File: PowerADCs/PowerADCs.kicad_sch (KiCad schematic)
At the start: 28 parts, among them J1 I2C_STANDARDQWIIC, J2 Conn_01x02_Female, J3 Conn_01x10_Female, J4 Conn_01x10_Female, J6 Conn_01x02_Female, J7 Conn_01x02_Female, U1 MCP3428, U2 MCP3428, U3 INA219AxD, U4 SY6280AAC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

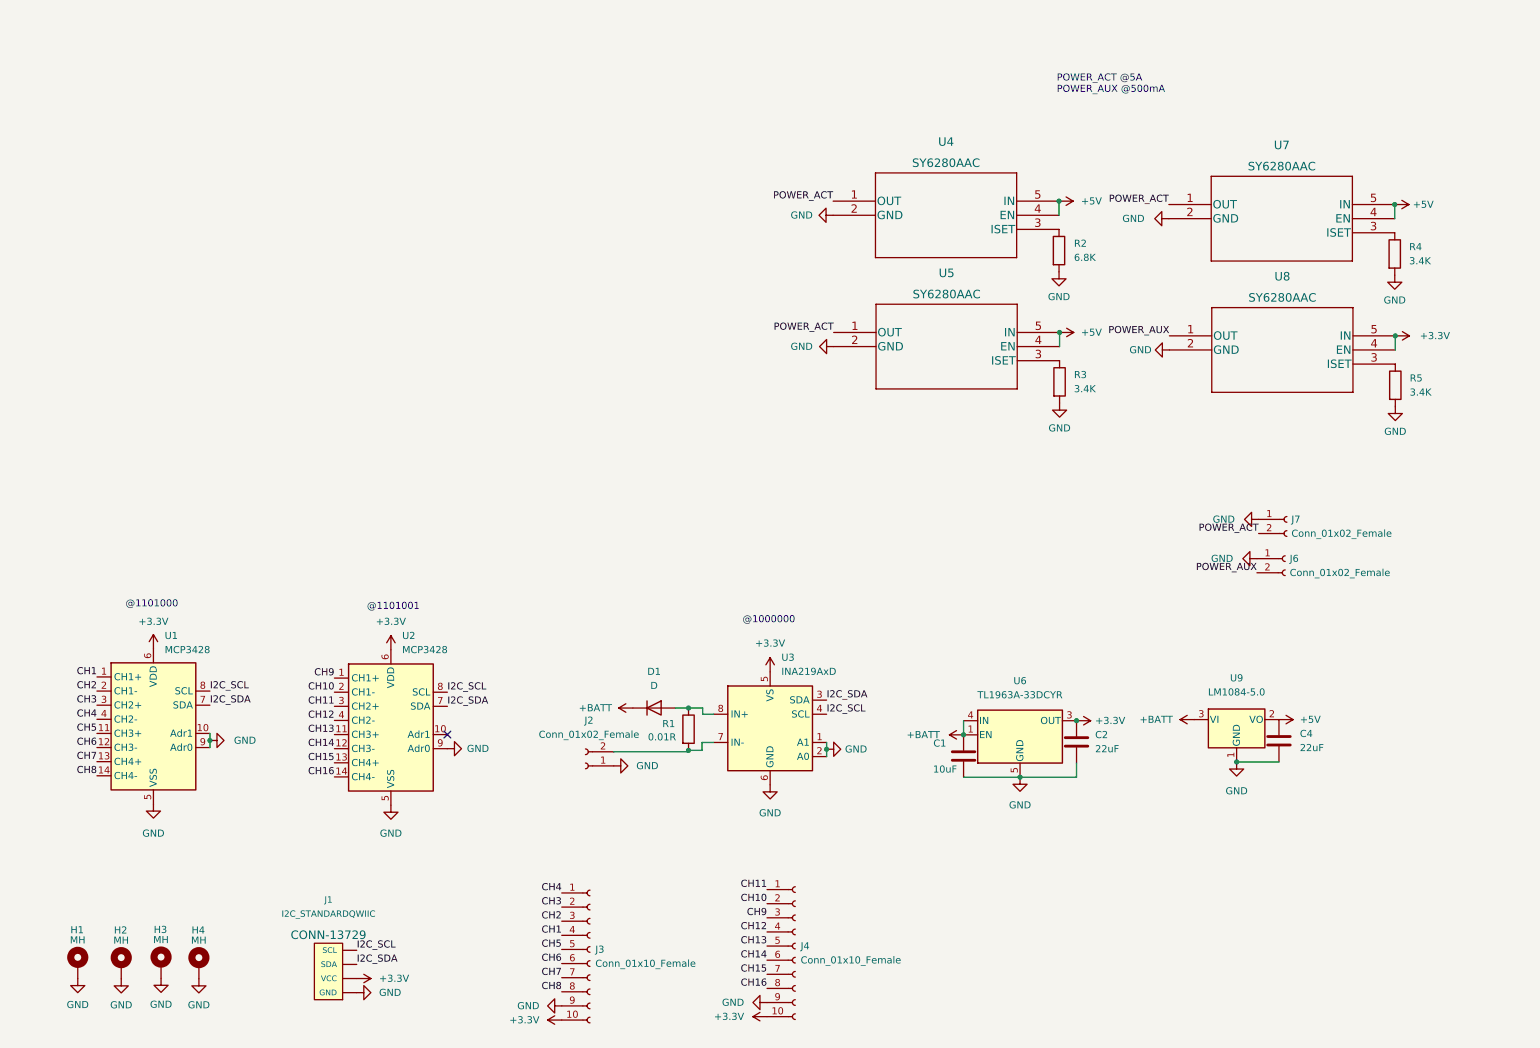
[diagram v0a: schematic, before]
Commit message: change ADC's and add seconde qwiic connector
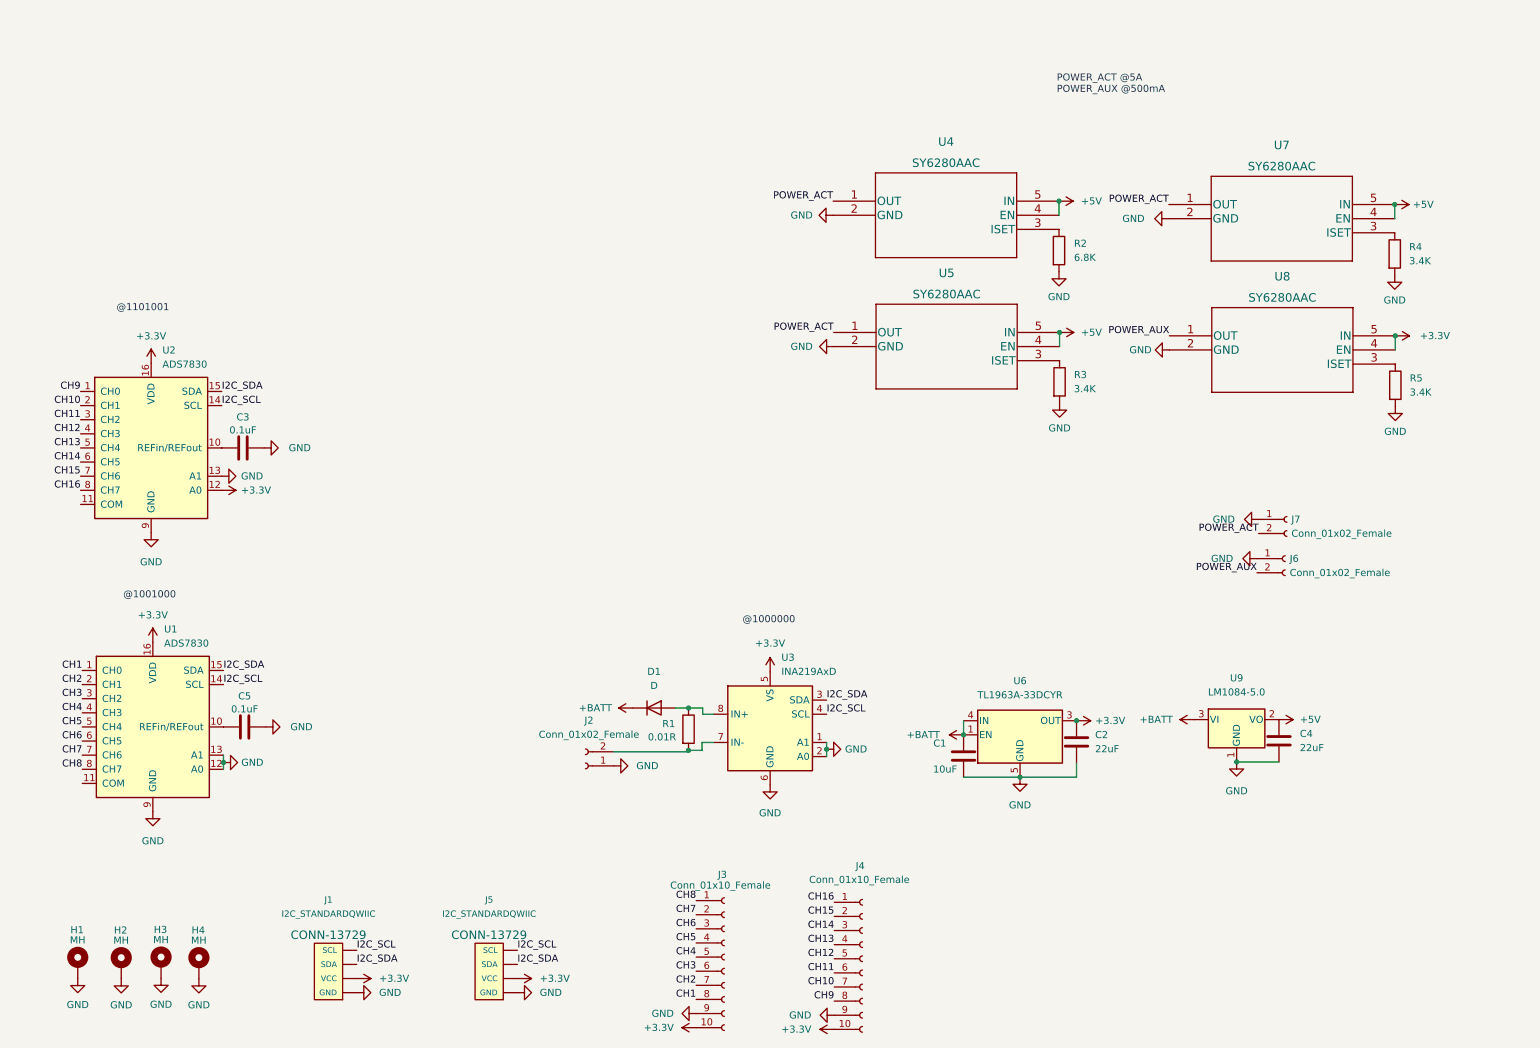
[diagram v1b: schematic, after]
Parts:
- removed U1, U2: MCP3428, Package_SO:TSSOP-14_4.4x5mm_P0.65mm, symbol Analog_ADC:MCP3428
- added C3, C5: 0.1uF, Capacitor_SMD:C_0402_1005Metric, symbol Device:C
- added J5: I2C_STANDARDQWIIC, Connectors:1X04_1MM_RA, symbol SparkFun-Connectors:I2C_STANDARDQWIIC
- added U1, U2: ADS7830, Package_SO:TSSOP-16_4.4x5mm_P0.65mm, symbol Analog_DAC:ADS7830
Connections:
- net +3V3: now also J5.2 (VCC), U1.16 (VDD), U2.12 (A0), U2.16 (VDD)
- net CH1: now also J3.8 (Pin_8), U1.1 (CH0); no longer J3.4 (Pin_4)
- net CH10: now also J4.7 (Pin_7), U2.2 (CH1); no longer J4.2 (Pin_2)
- net CH11: now also J4.6 (Pin_6), U2.3 (CH2); no longer J4.1 (Pin_1)
- net CH12: now also J4.5 (Pin_5), U2.4 (CH3); no longer J4.4 (Pin_4)
- net CH13: now also J4.4 (Pin_4), U2.5 (CH4); no longer J4.5 (Pin_5)
- net CH14: now also J4.3 (Pin_3), U2.6 (CH5); no longer J4.6 (Pin_6)
- net CH15: now also J4.2 (Pin_2), U2.7 (CH6); no longer J4.7 (Pin_7)
- net CH16: now also J4.1 (Pin_1), U2.8 (CH7); no longer J4.8 (Pin_8)
- net CH2: now also J3.7 (Pin_7), U1.2 (CH1); no longer J3.3 (Pin_3)
- net CH3: now also J3.6 (Pin_6), U1.3 (CH2); no longer J3.2 (Pin_2)
- net CH4: now also J3.5 (Pin_5), U1.4 (CH3); no longer J3.1 (Pin_1)
- net CH5: now also J3.4 (Pin_4), U1.5 (CH4); no longer J3.5 (Pin_5)
- net CH6: now also J3.3 (Pin_3), U1.6 (CH5); no longer J3.6 (Pin_6)
- net CH7: now also J3.2 (Pin_2), U1.7 (CH6); no longer J3.7 (Pin_7)
- net CH8: now also J3.1 (Pin_1), U1.8 (CH7); no longer J3.8 (Pin_8)
- net CH9: now also J4.8 (Pin_8), U2.1 (CH0); no longer J4.3 (Pin_3)
- net GND: now also C3.2, C5.2, J5.1 (GND), U1.12 (A0), U1.13 (A1), U1.9 (GND), U2.13 (A1), U2.9 (GND)
- net I2C_SCL: now also J5.4 (SCL), U1.14 (SCL), U2.14 (SCL)
- net I2C_SDA: now also J5.3 (SDA), U1.15 (SDA), U2.15 (SDA)
- new net: C3.1, U2.10 (REFin/REFout)
- new net: C5.1, U1.10 (REFin/REFout)
- no-connect marks 1 -> 0
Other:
- note added: "@1001000"
- note removed: "@1101000"
- moved on the sheet: J3, J4

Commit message: more silkscreen and fix resistor value for current limiter
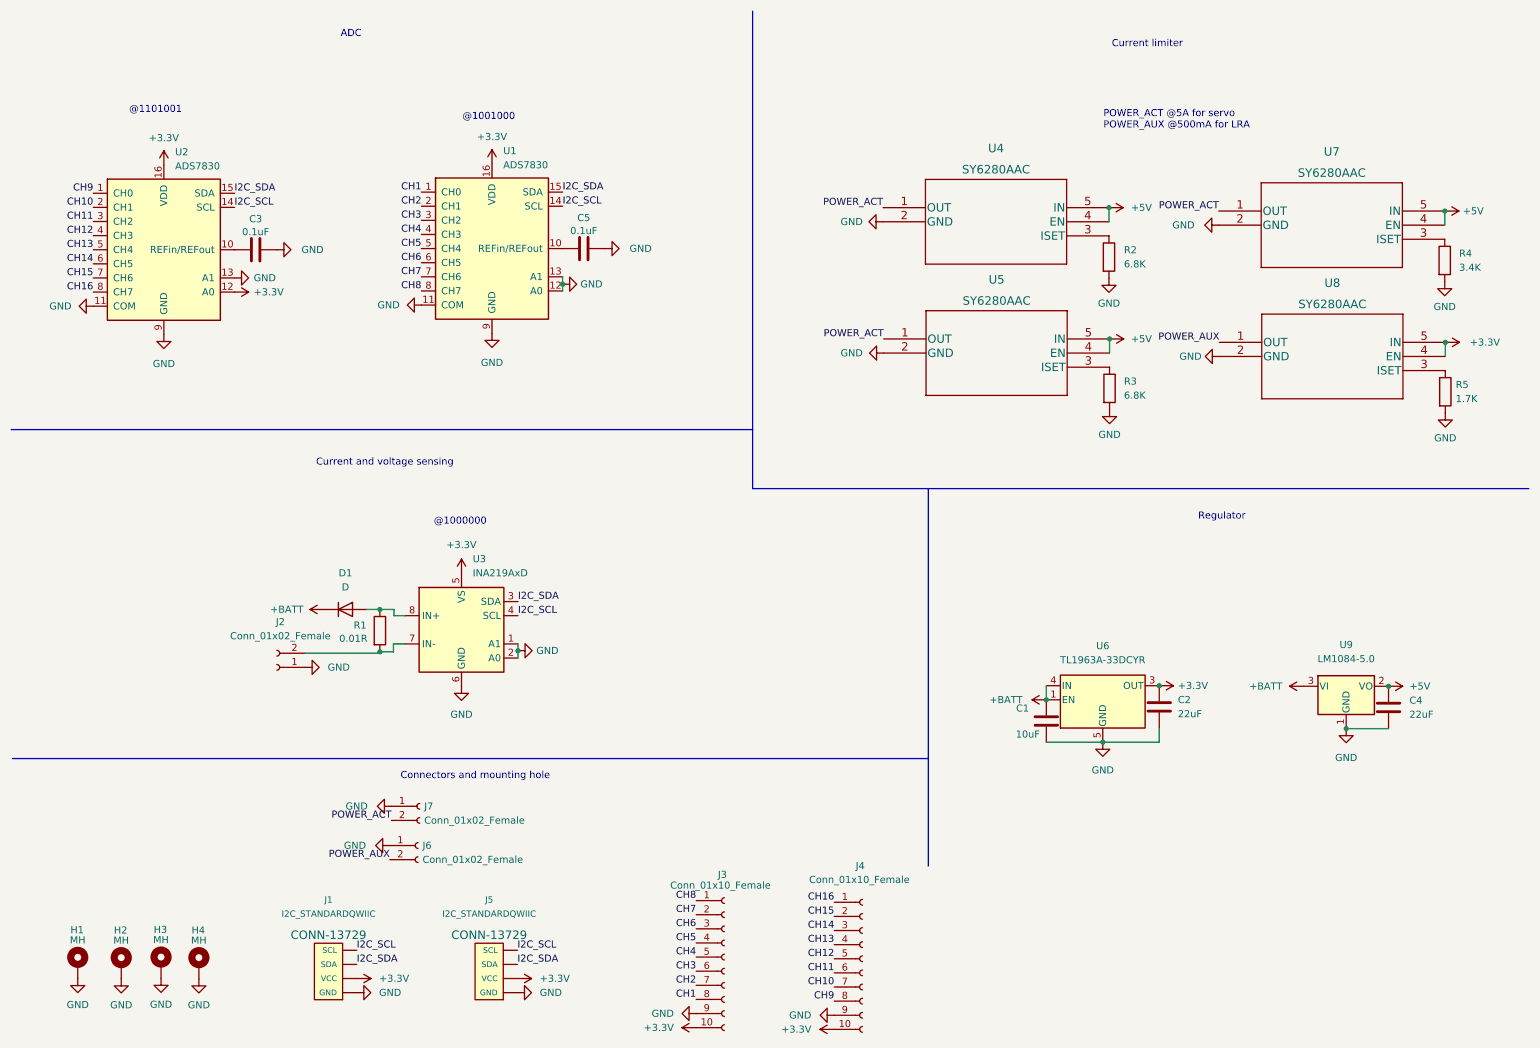
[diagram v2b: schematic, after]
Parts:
- R3: value 3.4K -> 6.8K
- R5: value 3.4K -> 1.7K
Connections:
- net GND: now also U1.11 (COM), U2.11 (COM)
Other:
- note added: "ADC"
- note added: "Connectors and mounting hole"
- note added: "Current and voltage sensing"
- note added: "Current limiter"
- note added: "POWER_ACT @5A for servo POWER_AUX @500mA for LRA"
- note added: "Regulator"
- note removed: "POWER_ACT @5A POWER_AUX @500mA"
- moved on the sheet: C1, C2, C3, C4, C5, D1, J2, J6, J7, R1, R2, R3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
